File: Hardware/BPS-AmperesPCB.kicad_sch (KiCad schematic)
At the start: 47 parts, among them IC1 INA241A5IDR, IC2 OPA396DCKR, IC5 AMC1350DWVR, J1 Discharge V_In, J2 PeripheralCAN, J3 Charge V_In, J4 PeripheralCAN, J5 Shunt Conn, U1 INA145UA/2K5, U7 TLV6001DCK

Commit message: scrutineering should be done, started on USB
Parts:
- removed C1: 1uF, Capacitor_SMD:C_0805_2012Metric, symbol Device:C
- removed C2, C4: 2.2uF, Capacitor_SMD:C_0805_2012Metric, symbol Device:C
- removed D1, D2: RBE01VYM6AFHTR, Parts:RBE01VYM6AFHTR, symbol RBE01:RBE01VYM6AFHTR
- removed H1: ShuntHole1, symbol Mechanical:MountingHole
- removed H2: ShuntHole2, symbol Mechanical:MountingHole
- removed J2, J4: PeripheralCAN, UTSVT_Connectors:Molex_Nano-Fit_105309-xx04_1x04_P2.50mm_Vertical, symbol utsvt-connectors:PeripheralCANConnector
- removed J3: Charge V_In, Connector_Molex:Molex_Micro-Fit_3.0_43650-0200_1x02_P3.00mm_Horizontal, symbol Connector_Generic:Conn_01x02
- removed J5: Shunt Conn, Connector_PinSocket_2.54mm:PinSocket_1x04_P2.54mm_Vertical, symbol Connector_Generic:Conn_01x04
- removed JP1: Scrutineering, symbol Jumper:Jumper_3_Bridged12
- removed R1, R2: ??, Resistor_SMD:R_0805_2012Metric, symbol Device:R
- removed R3: 4.8k, Resistor_SMD:R_0805_2012Metric, symbol Device:R_Small_US
- removed R5, R7: 2.4k, Resistor_SMD:R_0805_2012Metric, symbol Device:R_Small_US
- removed R8: 12k, Resistor_SMD:R_0805_2012Metric, symbol Device:R_Small_US
- removed R9: 1k, Resistor_SMD:R_0805_2012Metric, symbol Device:R_Small_US
- removed TP3: V_Out+, TestPoint:TestPoint_Pad_2.0x2.0mm, symbol Connector:TestPoint
- removed TP4: V-, TestPoint:TestPoint_Pad_2.0x2.0mm, symbol Connector:TestPoint
- removed U1: INA145UA/2K5, Parts:D8, symbol INA145:INA145UA_2K5
- removed VOut1: TestPoint, TestPoint:TestPoint_Keystone_5005-5009_Compact, symbol Connector:TestPoint
- added H3, H4, H5, H6: MountingHole, symbol Mechanical:MountingHole
- added J5: Shunt Resistor, symbol Connector_Generic:Conn_01x02
- added R1: 59, symbol Device:R_Small
- added R24: 34k, symbol Device:R_Small
- added SW2: Scrutineering, symbol Switch:SW_SPDT
- added TP13: V_In+, symbol Connector:TestPoint
- added TP14: V_In-, symbol Connector:TestPoint
- J1: value Discharge V_In -> Scrut In
- TP2: value V_In+ -> V_Out+; footprint TestPoint:TestPoint_Pad_2.0x2.0mm -> (none)
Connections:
- net SHUNT+: now also J5.1 (Pin_1), SW2.3 (C); no longer IC1.8 (IN+)
- net SHUNT-: now also J5.2 (Pin_2); no longer IC1.1 (IN-)
- net V_In+: now also R24.1, TP13.1; no longer TP2.1
- net V- renamed V_In-
- net V_In-: now also R1.2, TP14.1
- new net INPUT+: IC1.8 (IN+), SW2.2 (B)
- new net INPUT-: IC1.1 (IN-)
- new net V_Out: R1.1, R24.2, SW2.1 (A), TP2.1
- no-connect marks 1 -> 0
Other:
- added sheet USB (USB.kicad_sch)
- sheet CAN ports: added {CAN1}; removed CAN_HIGH, CAN_LOW, CAN_RX, CAN_TX
- sheet MCU ports: added {CAN1}, {USART1}; removed CAN_RX, CAN_TX
- note added: "(0.0017) V_in"
- note added: "250uOhm Shunt Resistor"
- note added: "2nd order lowpass Butterworth filter Cutoff frequency: 10 Hz Gain: 2.5 V/V Target Output voltage range: 0.1 - 3.2 V"
- note added: "Expected current range: -32A to +70A => Voltage range: -8 to 17.5 mV"
- note added: "Fixed Gain: 0.4 V/V Target Voltage Ranges: * Input: 0.1 - 3.2 V * Output: 0.04 - 1.28 V"
- note added: "Gain: 100 V/V Reference voltage (bias for discharge) Vref = 3.3 * [1k / (1k + 1.5k)] = 1.32 V * (70A * 250 uOhm * 100)V + Vref = 3.07 V * (-32A * 250 uOhm * 100)V + Vref = 0.52 V Maximum current range: -44 to +80A (0.1 to 3.2V output)"
- note added: "Scrutineering: Use switch to choose shunt or scrutineering input"
- note added: "Todo: make footprint"
- note removed: "(TBD) Shunt Resistor Between 1 and 2 - old value was 250 uOhm"
- note removed: "CAN"
- note removed: "Expected current range: -32A to +70A"
- note removed: "Fixed Gain: 0.4 V/V Target Input Voltage Range: 0.1 - 3.2 V Target Output Voltage Range: 0.04 - 1.28 V"
- note removed: "Gain: 100 V/V Target Input Voltage: Reference voltage (bias for discharge) - Vref = 3.3 * [1k / (1k + 1.5k)] = 1.32 V - (70A * 250 uOhm * 100)V + Vref = 3.05 V - (-32 * 250 uOhm * 100)V + Vref = 0.5 V Maximum current range: -44 to +80A (0.1V to 3.2V)"
- note removed: "Gain: 2.5 V/V Cutoff frequency: 10 Hz Target Output voltage range: 0.1 - 3.2 V"
- note removed: "Max Protected Current: 222A"
- note removed: "Maximum Voltage Protected: -2.7V - 6V"
- note removed: "Output Voltage Range: 0V - 3.25V"
- note removed: "Set cutoff frequency to < 100Hz"
- note removed: "TODO: add USB-C"
- note removed: "TODO: integrate jumper add documentation over how scrut works"
- note removed: "Total Gain (V/A): 0.027"
- moved on the sheet: IC1, J1, R22, R23, TP1, TP11, TP12, U7

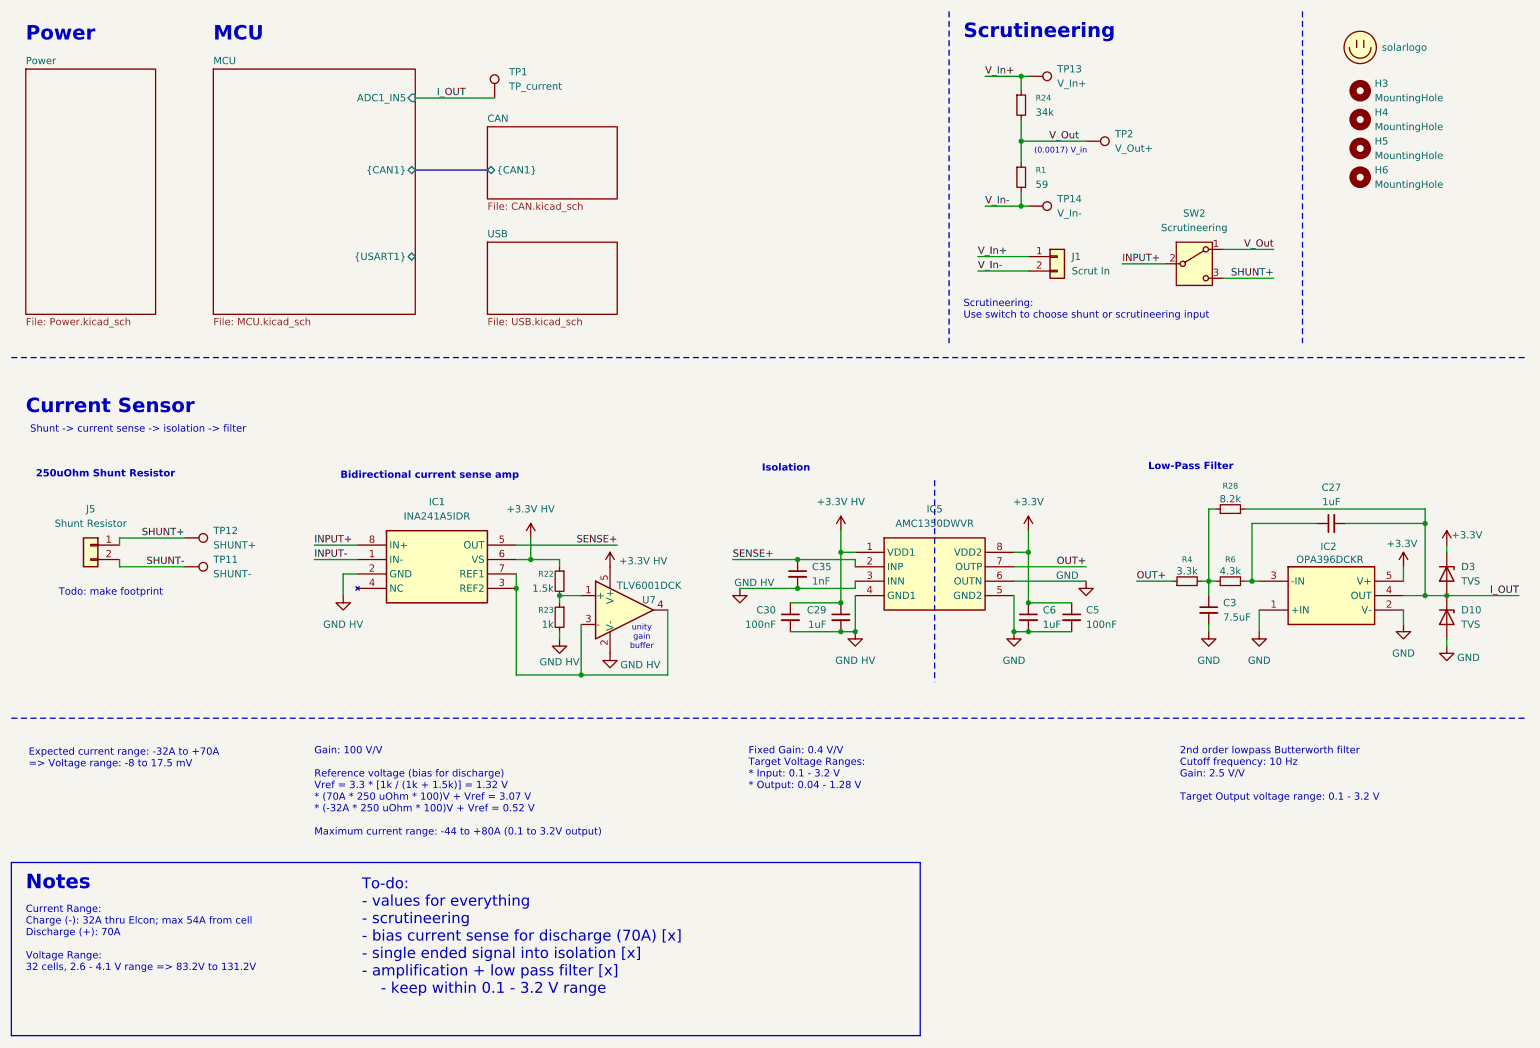
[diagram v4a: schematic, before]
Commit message: copied USB-C from psom
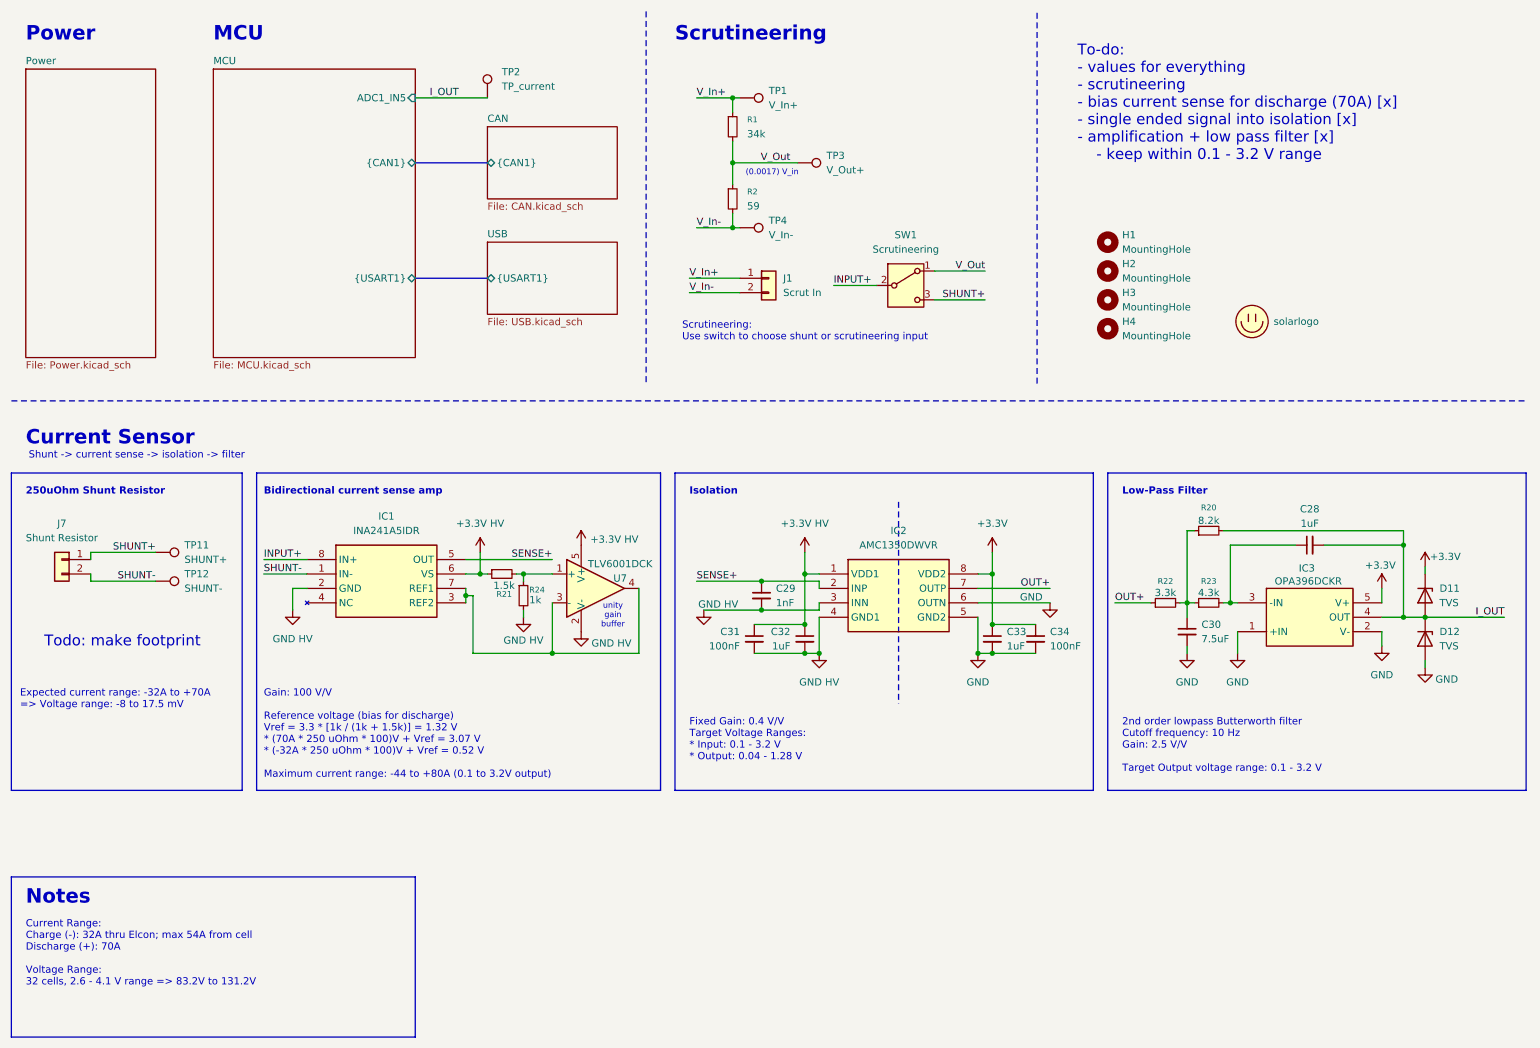
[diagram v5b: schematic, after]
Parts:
- renumbered C27 to C28, C35 to C29, C3 to C30, C30 to C31, C29 to C32, C6 to C33, C5 to C34, D3 to D11, D10 to D12, H3 to H1, H4 to H2, H5 to H3, H6 to H4, IC5 to IC2, IC2 to IC3, J5 to J7, LOGO2 to LOGO1, R24 to R1, R1 to R2, R28 to R20, R22 to R21, R4 to R22, R6 to R23, R23 to R24, SW2 to SW1, TP13 to TP1, TP12 to TP11, TP11 to TP12, TP1 to TP2, TP2 to TP3, TP14 to TP4
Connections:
- net INPUT- is gone; now on net SHUNT-: IC1.1 (IN-)
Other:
- sheet USB ports: added {USART1}; removed none
- moved on the sheet: C28, C29, C30, C31, C32, C33, C34, D11, D12, H1, H2, H3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

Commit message: something changed idk what though
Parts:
- renumbered C28 to C1, C29 to C2, C30 to C3, C31 to C4, C32 to C5, C33 to C6, C34 to C7, D11 to D1, D12 to D2, J7 to J2, R20 to R3, R21 to R4, R24 to R5, R22 to R6, R23 to R7, TP2 to TP1, TP1 to TP2, TP11 to TP5, TP12 to TP6, U7 to U1
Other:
- note added: "To-do: - footprint / finalize parts - scrutineering [x] - bias current sense for discharge (70A) [x] - single ended signal into isolation [x] - amplification + low pass filter [x] - keep within 0.1 - 3.2 V range"
- note removed: "To-do: - values for everything - scrutineering - bias current sense for discharge (70A) [x] - single ended signal into isolation [x] - amplification + low pass filter [x] - keep within 0.1 - 3.2 V range"

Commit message: sch almost done
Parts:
- LOGO1: footprint UTSVT_Logos:Hallock_Image_Small -> (none)
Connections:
- net SHUNT+: now also SW1.1 (A); no longer SW1.3 (C)
- net V_Out: now also SW1.3 (C); no longer SW1.1 (A)
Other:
- note added: "Add justification"
- note added: "Scrutineering: - Pass in voltage from scrutineering board; use switch to select btwn shunt / scrutineering Details: - Input+ is tied to either shunt or scrutineering input - Input- = Shunt- = effectively GND (correct me if wrong)"
- note added: "To-do: - footprints - specific part version for current sense, shunt - scrutineering [x] - bias current sense for discharge (70A) [x] - single ended signal into isolation [x] - amplification + low pass filter [x] - keep within 0.1 - 3.2 V range"
- note removed: "Scrutineering: Use switch to choose shunt or scrutineering input"
- note removed: "To-do: - footprint / finalize parts - scrutineering [x] - bias current sense for discharge (70A) [x] - single ended signal into isolation [x] - amplification + low pass filter [x] - keep within 0.1 - 3.2 V range"
- moved on the sheet: C1, C2, C3, C4, C5, C6, C7, D1, D2, H1, H2, H3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

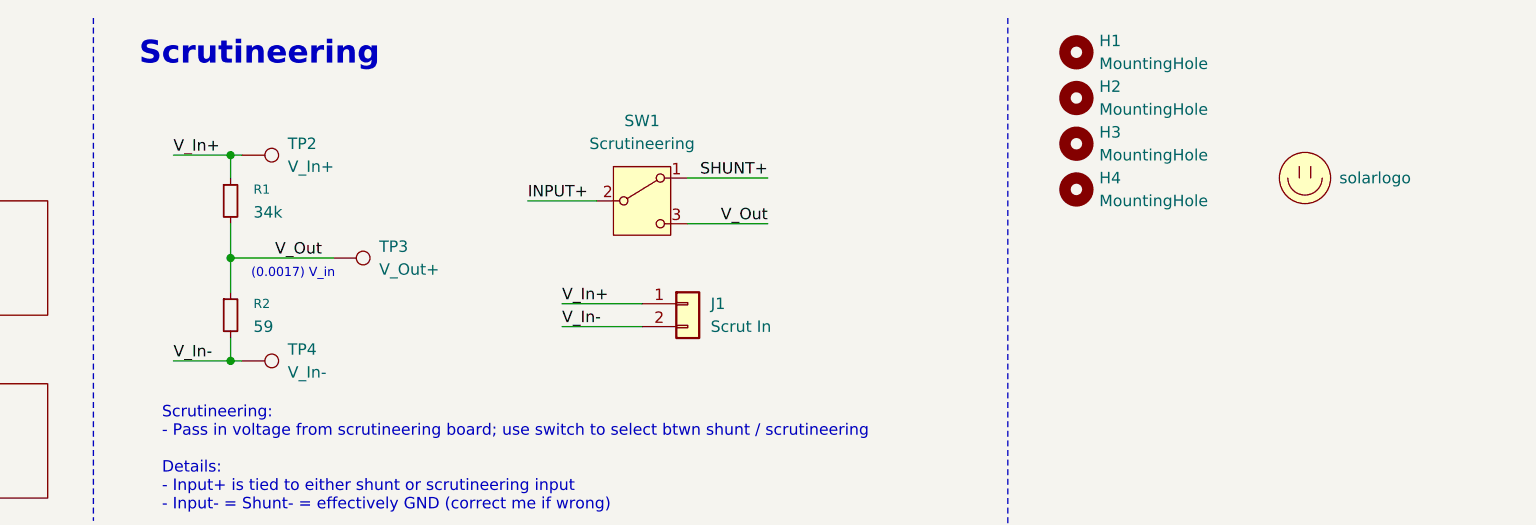
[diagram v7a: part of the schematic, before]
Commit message: 0603 footprints
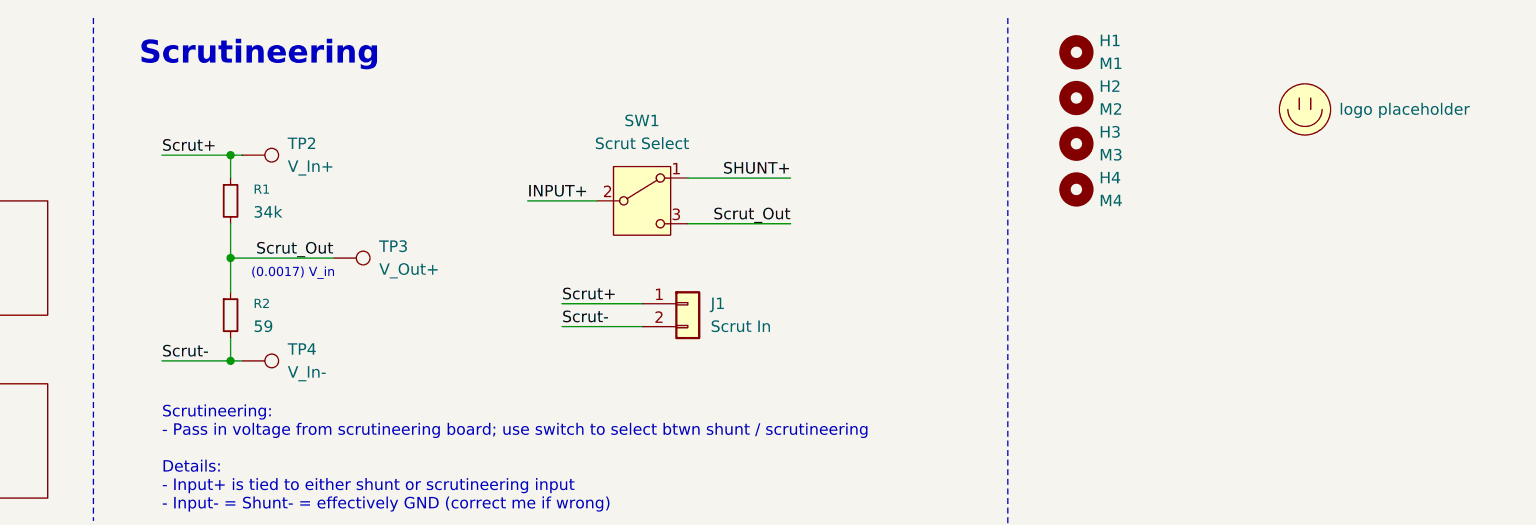
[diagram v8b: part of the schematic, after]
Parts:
- C1, C2, C3, C4, C5, C6, C7: footprint (none) -> Capacitor_SMD:C_0603_1608Metric_Pad1.08x0.95mm_HandSolder
- H1: value MountingHole -> M1; footprint (none) -> MountingHole:MountingHole_3.2mm_M3_DIN965_Pad_TopBottom
- H2: value MountingHole -> M2; footprint (none) -> MountingHole:MountingHole_3.2mm_M3_DIN965_Pad_TopBottom
- H3: value MountingHole -> M3; footprint (none) -> MountingHole:MountingHole_3.2mm_M3_DIN965_Pad_TopBottom
- H4: value MountingHole -> M4; footprint (none) -> MountingHole:MountingHole_3.2mm_M3_DIN965_Pad_TopBottom
- IC2: footprint SOIC127P1150X280-8N -> Parts:AMC1350DWVR
- IC3: footprint SOT65P210X110-5N -> Parts:SOT65P210X110-5N
- LOGO1: value solarlogo -> logo placeholder; footprint (none) -> UTSVT_Logos:LHRs_LOGO
- R1, R2, R3, R4, R5, R6, R7: footprint (none) -> Resistor_SMD:R_0603_1608Metric_Pad0.98x0.95mm_HandSolder
- SW1: value Scrutineering -> Scrut Select
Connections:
- net V_In+ renamed Scrut+
- net V_In- renamed Scrut-
- net V_Out renamed Scrut_Out
